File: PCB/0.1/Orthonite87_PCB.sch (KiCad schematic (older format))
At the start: 197 parts

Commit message: PCB schematic updates
add libraries
 schematic progress
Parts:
- added BZ?: Buzzer, PKMCS0909E4000-R1:PKMCS, symbol Keyboard-rescue:Buzzer-Device
- added C? (x2): 10u, keyboard_parts:C_1608, symbol Keyboard-rescue:C-Device
- added C? (x2): 1u, keyboard_parts:C_1608, symbol Keyboard-rescue:C-Device
- added C? (x29): 100n, keyboard_parts:C_1608, symbol Keyboard-rescue:C-Device
- added C? (x2): 4u7, keyboard_parts:C_1608, symbol Keyboard-rescue:C-Device
- added C? (x2): 15p, keyboard_parts:C_1608, symbol Keyboard-rescue:C-Device
- added D?: 1N4148, 1N4148_SOD-123_:SOD3716X135N, symbol Keyboard-rescue:D_Small-Device
- added D?: LE_RED, josh-led:LED_0603_1608Metric_45_noSilk, symbol Keyboard-rescue:LED-Device
- added F?: 500mA, josh-passives-smt:Fuse_0805_2012Metric, symbol Keyboard-rescue:Polyfuse-Device
- added J?: SWD, josh-connectors:STM_4_PIN_THT_Staggered, symbol Keyboard-rescue:Conn_01x04_Male-Connector
- added Q?: DTC123J, DTC123JKAT146:SOT95P280X100-3N, symbol Keyboard-rescue:DTC123J-Transistor_BJT
- added R? (x2): 5k1, keyboard_parts:R_1608, symbol Keyboard-rescue:R-Device
- added R?: 100K, keyboard_parts:R_1608, symbol Keyboard-rescue:R-Device
- added R?: 5K1, keyboard_parts:R_1608, symbol Keyboard-rescue:R-Device
- added SW?: EVQPUL02K, josh-buttons-switches:Panasonic_EVQPUL_EVQPUC, symbol Keyboard-rescue:SW_Push-Switch
- added U?: USBLC6-2SC6, Package_TO_SOT_SMD:SOT-23-6, symbol josh-ic:USBLC6-2SC6
- added U?: AP2112K-3.3, Package_TO_SOT_SMD:SOT-23-5, symbol Keyboard-rescue:AP2112K-3.3-Regulator_Linear
- added U?: STM32F303RCTx, Package_QFP:LQFP-64_10x10mm_P0.5mm, symbol Keyboard-rescue:STM32F303RCTx-MCU_ST_STM32F3
- added Y?: 8MHz, josh-oscillators:Crystal_SMD_3225-4Pin_3.2x2.5mm, symbol Keyboard-rescue:Crystal_GND24-Device
- J?: Notes (none) -> Sub: USB4105-GF-A (available at Digikey)
- gave numbers to parts that had none: 1
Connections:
- net labels added: +3V3-power, +5V-power, BOOT0, BUZZER, GND, SWDCLK, SWDIO, USB+, USB-, USB_D+, USB_D-, VBUS-power, XTAL_0, XTAL_1, nRST
- net labels removed: GND-power
- wire segments 410 -> 593
- no-connect marks 0 -> 2
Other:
- note added: "Bangers r us"
- note added: "DFU/Reset"
- note added: "Programming"
- note added: "The Brains"
- note added: "USB/Power"
- moved on the sheet: D?, K?, SW?

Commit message: Schematic update
Near finished with rev0.1
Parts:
- removed K? (x2): KEYSW, josh-keyboard_W:MXOnly-1U-NoLED, symbol josh-keyboard:MX-NoLED
- added D1, D10, D11, D12, D13, D14, D15, D16, D17, D18, D19, D2, D20, D3, D4, D5, D6, D7, D8, D9: WS2812B, LED_SMD:LED_WS2812B_PLCC4_5.0x5.0mm_P3.2mm, symbol LED:WS2812B
- added D21, D22, D23, D24: SK6812-MINI-E, josh-led:SK8612-MINI-E, symbol josh-led:SK6812-MINI-E
- added D_100, D_15, D_32, D_49, D_66, D_83: 1N4148, 1N4148_SOD-123_:SOD3716X135N, symbol Keyboard-rescue:D_Small-Device
- added K_108: 5,18, josh-keyboard:MXOnly-1U-NoLED, symbol josh-keyboard:MX-NoLED
- added K_16: 0,14, josh-keyboard:MXOnly-1U-NoLED, symbol josh-keyboard:MX-NoLED
- added K_33: 1,17, josh-keyboard:MXOnly-1U-NoLED, symbol josh-keyboard:MX-NoLED
- added K_51: 2,17, josh-keyboard:MXOnly-1U-NoLED, symbol josh-keyboard:MX-NoLED
- added K_53: 3,17, josh-keyboard:MXOnly-1U-NoLED, symbol josh-keyboard:MX-NoLED
- added K_70: 3,18, josh-keyboard:MXOnly-2U-NoLED, symbol josh-keyboard:MX-NoLED
- added K_72: 4,17, josh-keyboard:MXOnly-1U-NoLED, symbol josh-keyboard:MX-NoLED
- added K_89: 4,18, josh-keyboard:MXOnly-2U-NoLED, symbol josh-keyboard:MX-NoLED
- added Q1: BSS138, Package_TO_SOT_SMD:SOT-23, symbol Keyboard-rescue:BSS138-Transistor_FET
- added R1, R2: 10K, keyboard_parts:R_1608, symbol Keyboard-rescue:R-Device
- added R5: 1K5, Resistor_SMD:R_0603_1608Metric, symbol Device:R_Small
- BZ1: renamed from BZ?; footprint PKMCS0909E4000-R1:PKMCS -> Buzzer_Beeper:Buzzer_Murata_PKMCS0909E4000-R1
- K_1: renamed from K?; value Encoder_MX -> 0,15
- K_10: renamed from K?; value KEYSW -> 0,8; footprint josh-keyboard_W:MXOnly-1U-NoLED -> josh-keyboard:MXOnly-1U-NoLED
- K_100: renamed from K?; value KEYSW -> 5,9; footprint josh-keyboard_W:MXOnly-1U-NoLED -> josh-keyboard:MXOnly-1U-NoLED
- K_101: renamed from K?; value KEYSW -> 5,10; footprint josh-keyboard_W:MXOnly-1U-NoLED -> josh-keyboard:MXOnly-1U-NoLED
- K_102: renamed from K?; value KEYSW -> 5,11; footprint josh-keyboard_W:MXOnly-1U-NoLED -> josh-keyboard:MXOnly-1U-NoLED
- K_103: renamed from K?; value KEYSW -> 5,12; footprint josh-keyboard_W:MXOnly-1U-NoLED -> josh-keyboard:MXOnly-1U-NoLED
- K_104: renamed from K?; value KEYSW -> 5,14; footprint josh-keyboard_W:MXOnly-1U-NoLED -> josh-keyboard:MXOnly-3U-ReversedStabilizers-NoLED
- K_105: renamed from K?; value KEYSW -> 5,15; footprint josh-keyboard_W:MXOnly-1U-NoLED -> josh-keyboard:MXOnly-1U-NoLED
- K_106: renamed from K?; value KEYSW -> 5,16; footprint josh-keyboard_W:MXOnly-1U-NoLED -> josh-keyboard:MXOnly-1U-NoLED
- K_107: renamed from K?; value KEYSW -> 5,17; footprint josh-keyboard_W:MXOnly-1U-NoLED -> josh-keyboard:MXOnly-1U-NoLED
- K_11: renamed from K?; value KEYSW -> 0,9; footprint josh-keyboard_W:MXOnly-1U-NoLED -> josh-keyboard:MXOnly-1U-NoLED
- K_12: renamed from K?; value KEYSW -> 0,10; footprint josh-keyboard_W:MXOnly-1U-NoLED -> josh-keyboard:MXOnly-1U-NoLED
- K_13: renamed from K?; value KEYSW -> 0,11; footprint josh-keyboard_W:MXOnly-1U-NoLED -> josh-keyboard:MXOnly-1U-NoLED
- K_14: renamed from K?; value KEYSW -> 0,12; footprint josh-keyboard_W:MXOnly-1U-NoLED -> josh-keyboard:MXOnly-1U-NoLED
- K_15: renamed from K?; value KEYSW -> 0,13; footprint josh-keyboard_W:MXOnly-1U-NoLED -> josh-keyboard:MXOnly-1U-NoLED
- K_17: renamed from K?; value KEYSW -> 1,15; footprint josh-keyboard_W:MXOnly-1U-NoLED -> josh-keyboard:MXOnly-1U-NoLED
- K_18: renamed from K?; value KEYSW -> 1,1; footprint josh-keyboard_W:MXOnly-1U-NoLED -> josh-keyboard:MXOnly-1U-NoLED
- K_19: renamed from K?; value KEYSW -> 1,2; footprint josh-keyboard_W:MXOnly-1U-NoLED -> josh-keyboard:MXOnly-1U-NoLED
- K_2: renamed from K?; value KEYSW -> 0,0; footprint josh-keyboard_W:MXOnly-1U-NoLED -> josh-keyboard:MXOnly-1U-NoLED
- K_20: renamed from K?; value KEYSW -> 1,3; footprint josh-keyboard_W:MXOnly-1U-NoLED -> josh-keyboard:MXOnly-1U-NoLED
- K_21: renamed from K?; value KEYSW -> 1,4; footprint josh-keyboard_W:MXOnly-1U-NoLED -> josh-keyboard:MXOnly-1U-NoLED
- K_22: renamed from K?; value KEYSW -> 1,5; footprint josh-keyboard_W:MXOnly-1U-NoLED -> josh-keyboard:MXOnly-1U-NoLED
- K_23: renamed from K?; value KEYSW -> 1,6; footprint josh-keyboard_W:MXOnly-1U-NoLED -> josh-keyboard:MXOnly-1U-NoLED
- K_24: renamed from K?; value KEYSW -> 1,7; footprint josh-keyboard_W:MXOnly-1U-NoLED -> josh-keyboard:MXOnly-1U-NoLED
- K_25: renamed from K?; value KEYSW -> 1,8; footprint josh-keyboard_W:MXOnly-1U-NoLED -> josh-keyboard:MXOnly-1U-NoLED
- K_26: renamed from K?; value KEYSW -> 1,9; footprint josh-keyboard_W:MXOnly-1U-NoLED -> josh-keyboard:MXOnly-1U-NoLED
- K_27: renamed from K?; value KEYSW -> 1,10; footprint josh-keyboard_W:MXOnly-1U-NoLED -> josh-keyboard:MXOnly-1U-NoLED
- K_28: renamed from K?; value KEYSW -> 1,11; footprint josh-keyboard_W:MXOnly-1U-NoLED -> josh-keyboard:MXOnly-1U-NoLED
- K_29: renamed from K?; value KEYSW -> 1,12; footprint josh-keyboard_W:MXOnly-1U-NoLED -> josh-keyboard:MXOnly-1U-NoLED
- K_3: renamed from K?; value KEYSW -> 0,1; footprint josh-keyboard_W:MXOnly-1U-NoLED -> josh-keyboard:MXOnly-1U-NoLED
- K_30: renamed from K?; value KEYSW -> 1,13; footprint josh-keyboard_W:MXOnly-1U-NoLED -> josh-keyboard:MXOnly-1U-NoLED
- K_31: renamed from K?; value KEYSW -> 1,14; footprint josh-keyboard_W:MXOnly-1U-NoLED -> josh-keyboard:MXOnly-1U-NoLED
- K_32: renamed from K?; value KEYSW -> 1,16; footprint josh-keyboard_W:MXOnly-1U-NoLED -> josh-keyboard:MXOnly-2U-NoLED
- K_34: renamed from K?; value KEYSW -> 2,1; footprint josh-keyboard_W:MXOnly-1U-NoLED -> josh-keyboard:MXOnly-1U-NoLED
- K_35: renamed from K?; value KEYSW -> 2,0; footprint josh-keyboard_W:MXOnly-1U-NoLED -> josh-keyboard:MXOnly-1U-NoLED
- K_36: renamed from K?; value KEYSW -> 2,2; footprint josh-keyboard_W:MXOnly-1U-NoLED -> josh-keyboard:MXOnly-2U-NoLED
- K_37: renamed from K?; value KEYSW -> 2,3; footprint josh-keyboard_W:MXOnly-1U-NoLED -> josh-keyboard:MXOnly-1U-NoLED
- K_38: renamed from K?; value KEYSW -> 2,4; footprint josh-keyboard_W:MXOnly-1U-NoLED -> josh-keyboard:MXOnly-1U-NoLED
- K_39: renamed from K?; value KEYSW -> 2,5; footprint josh-keyboard_W:MXOnly-1U-NoLED -> josh-keyboard:MXOnly-1U-NoLED
- K_4: renamed from K?; value KEYSW -> 0,2; footprint josh-keyboard_W:MXOnly-1U-NoLED -> josh-keyboard:MXOnly-1U-NoLED
- K_40: renamed from K?; value KEYSW -> 2,6; footprint josh-keyboard_W:MXOnly-1U-NoLED -> josh-keyboard:MXOnly-1U-NoLED
- K_41: renamed from K?; value KEYSW -> 2,7; footprint josh-keyboard_W:MXOnly-1U-NoLED -> josh-keyboard:MXOnly-1U-NoLED
- K_42: renamed from K?; value KEYSW -> 2,8; footprint josh-keyboard_W:MXOnly-1U-NoLED -> josh-keyboard:MXOnly-1U-NoLED
- K_43: renamed from K?; value KEYSW -> 2,9; footprint josh-keyboard_W:MXOnly-1U-NoLED -> josh-keyboard:MXOnly-1U-NoLED
- K_44: renamed from K?; value KEYSW -> 2,10; footprint josh-keyboard_W:MXOnly-1U-NoLED -> josh-keyboard:MXOnly-1U-NoLED
- K_45: renamed from K?; value KEYSW -> 2,11; footprint josh-keyboard_W:MXOnly-1U-NoLED -> josh-keyboard:MXOnly-1U-NoLED
- K_46: renamed from K?; value KEYSW -> 2,12; footprint josh-keyboard_W:MXOnly-1U-NoLED -> josh-keyboard:MXOnly-1U-NoLED
- K_47: renamed from K?; value KEYSW -> 2,13; footprint josh-keyboard_W:MXOnly-1U-NoLED -> josh-keyboard:MXOnly-1U-NoLED
- K_48: renamed from K?; value KEYSW -> 2,14; footprint josh-keyboard_W:MXOnly-1U-NoLED -> josh-keyboard:MXOnly-1U-NoLED
- K_49: renamed from K?; value KEYSW -> 2,15; footprint josh-keyboard_W:MXOnly-1U-NoLED -> josh-keyboard:MXOnly-1U-NoLED
- K_5: renamed from K?; value KEYSW -> 0,3; footprint josh-keyboard_W:MXOnly-1U-NoLED -> josh-keyboard:MXOnly-1U-NoLED
- K_50: renamed from K?; value KEYSW -> 2,16; footprint josh-keyboard_W:MXOnly-1U-NoLED -> josh-keyboard:MXOnly-1U-NoLED
- K_52: renamed from K?; value KEYSW -> 3,1; footprint josh-keyboard_W:MXOnly-1U-NoLED -> josh-keyboard:MXOnly-1U-NoLED
- K_54: renamed from K?; value KEYSW -> 3,0; footprint josh-keyboard_W:MXOnly-1U-NoLED -> josh-keyboard:MXOnly-1U-NoLED
- K_55: renamed from K?; value KEYSW -> 3,2; footprint josh-keyboard_W:MXOnly-1U-NoLED -> josh-keyboard:MXOnly-2U-NoLED
- K_56: renamed from K?; value KEYSW -> 3,3; footprint josh-keyboard_W:MXOnly-1U-NoLED -> josh-keyboard:MXOnly-1U-NoLED
- K_57: renamed from K?; value KEYSW -> 3,4; footprint josh-keyboard_W:MXOnly-1U-NoLED -> josh-keyboard:MXOnly-1U-NoLED
- K_58: renamed from K?; value KEYSW -> 3,5; footprint josh-keyboard_W:MXOnly-1U-NoLED -> josh-keyboard:MXOnly-1U-NoLED
- K_59: renamed from K?; value KEYSW -> 3,6; footprint josh-keyboard_W:MXOnly-1U-NoLED -> josh-keyboard:MXOnly-1U-NoLED
- K_6: renamed from K?; value KEYSW -> 0,4; footprint josh-keyboard_W:MXOnly-1U-NoLED -> josh-keyboard:MXOnly-1U-NoLED
- K_60: renamed from K?; value KEYSW -> 3,7; footprint josh-keyboard_W:MXOnly-1U-NoLED -> josh-keyboard:MXOnly-1U-NoLED
- K_61: renamed from K?; value KEYSW -> 3,8; footprint josh-keyboard_W:MXOnly-1U-NoLED -> josh-keyboard:MXOnly-1U-NoLED
- K_62: renamed from K?; value KEYSW -> 3,9; footprint josh-keyboard_W:MXOnly-1U-NoLED -> josh-keyboard:MXOnly-1U-NoLED
- K_63: renamed from K?; value KEYSW -> 3,10; footprint josh-keyboard_W:MXOnly-1U-NoLED -> josh-keyboard:MXOnly-1U-NoLED
- K_64: renamed from K?; value KEYSW -> 3,11; footprint josh-keyboard_W:MXOnly-1U-NoLED -> josh-keyboard:MXOnly-1U-NoLED
- K_65: renamed from K?; value KEYSW -> 3,12; footprint josh-keyboard_W:MXOnly-1U-NoLED -> josh-keyboard:MXOnly-1U-NoLED
- K_66: renamed from K?; value KEYSW -> 3,13; footprint josh-keyboard_W:MXOnly-1U-NoLED -> josh-keyboard:MXOnly-1U-NoLED
- K_67: renamed from K?; value KEYSW -> 3,14; footprint josh-keyboard_W:MXOnly-1U-NoLED -> josh-keyboard:MXOnly-1U-NoLED
- K_68: renamed from K?; value KEYSW -> 3,15; footprint josh-keyboard_W:MXOnly-1U-NoLED -> josh-keyboard:MXOnly-1U-NoLED
- K_69: renamed from K?; value KEYSW -> 3,16; footprint josh-keyboard_W:MXOnly-1U-NoLED -> josh-keyboard:MXOnly-1U-NoLED
- K_7: renamed from K?; value KEYSW -> 0,5; footprint josh-keyboard_W:MXOnly-1U-NoLED -> josh-keyboard:MXOnly-1U-NoLED
- K_71: renamed from K?; value KEYSW -> 4,1; footprint josh-keyboard_W:MXOnly-1U-NoLED -> josh-keyboard:MXOnly-1U-NoLED
- K_73: renamed from K?; value KEYSW -> 4,0; footprint josh-keyboard_W:MXOnly-1U-NoLED -> josh-keyboard:MXOnly-1U-NoLED
- K_74: renamed from K?; value KEYSW -> 4,2; footprint josh-keyboard_W:MXOnly-1U-NoLED -> josh-keyboard:MXOnly-2U-NoLED
- K_75: renamed from K?; value KEYSW -> 4,3; footprint josh-keyboard_W:MXOnly-1U-NoLED -> josh-keyboard:MXOnly-1U-NoLED
- K_76: renamed from K?; value KEYSW -> 4,4; footprint josh-keyboard_W:MXOnly-1U-NoLED -> josh-keyboard:MXOnly-1U-NoLED
- K_77: renamed from K?; value KEYSW -> 4,5; footprint josh-keyboard_W:MXOnly-1U-NoLED -> josh-keyboard:MXOnly-1U-NoLED
- K_78: renamed from K?; value KEYSW -> 4,6; footprint josh-keyboard_W:MXOnly-1U-NoLED -> josh-keyboard:MXOnly-1U-NoLED
- K_79: renamed from K?; value KEYSW -> 4,7; footprint josh-keyboard_W:MXOnly-1U-NoLED -> josh-keyboard:MXOnly-1U-NoLED
- K_8: renamed from K?; value KEYSW -> 0,6; footprint josh-keyboard_W:MXOnly-1U-NoLED -> josh-keyboard:MXOnly-1U-NoLED
- K_80: renamed from K?; value KEYSW -> 4,8; footprint josh-keyboard_W:MXOnly-1U-NoLED -> josh-keyboard:MXOnly-1U-NoLED
- K_81: renamed from K?; value KEYSW -> 4,9; footprint josh-keyboard_W:MXOnly-1U-NoLED -> josh-keyboard:MXOnly-1U-NoLED
- K_82: renamed from K?; value KEYSW -> 4,10; footprint josh-keyboard_W:MXOnly-1U-NoLED -> josh-keyboard:MXOnly-1U-NoLED
- K_83: renamed from K?; value KEYSW -> 4,11; footprint josh-keyboard_W:MXOnly-1U-NoLED -> josh-keyboard:MXOnly-1U-NoLED
- K_84: renamed from K?; value KEYSW -> 4,12; footprint josh-keyboard_W:MXOnly-1U-NoLED -> josh-keyboard:MXOnly-1U-NoLED
- K_85: renamed from K?; value KEYSW -> 4,13; footprint josh-keyboard_W:MXOnly-1U-NoLED -> josh-keyboard:MXOnly-1U-NoLED
- K_86: renamed from K?; value KEYSW -> 4,14; footprint josh-keyboard_W:MXOnly-1U-NoLED -> josh-keyboard:MXOnly-1U-NoLED
- K_87: renamed from K?; value KEYSW -> 4,15; footprint josh-keyboard_W:MXOnly-1U-NoLED -> josh-keyboard:MXOnly-1U-NoLED
- K_88: renamed from K?; value KEYSW -> 4,16; footprint josh-keyboard_W:MXOnly-1U-NoLED -> josh-keyboard:MXOnly-1U-NoLED
- K_9: renamed from K?; value KEYSW -> 0,7; footprint josh-keyboard_W:MXOnly-1U-NoLED -> josh-keyboard:MXOnly-1U-NoLED
- K_90: renamed from K?; value KEYSW -> 5,4; footprint josh-keyboard_W:MXOnly-1U-NoLED -> josh-keyboard:MXOnly-1U-NoLED
- K_91: renamed from K?; value KEYSW -> 5,13; footprint josh-keyboard_W:MXOnly-1U-NoLED -> josh-keyboard:MXOnly-1U-NoLED
- K_92: renamed from K?; value KEYSW -> 5,0; footprint josh-keyboard_W:MXOnly-1U-NoLED -> josh-keyboard:MXOnly-1U-NoLED
- K_93: renamed from K?; value KEYSW -> 5,1; footprint josh-keyboard_W:MXOnly-1U-NoLED -> josh-keyboard:MXOnly-1U-NoLED
- K_94: renamed from K?; value KEYSW -> 5,2; footprint josh-keyboard_W:MXOnly-1U-NoLED -> josh-keyboard:MXOnly-1U-NoLED
- K_95: renamed from K?; value KEYSW -> 5,3; footprint josh-keyboard_W:MXOnly-1U-NoLED -> josh-keyboard:MXOnly-1U-NoLED
- K_96: renamed from K?; value KEYSW -> 5,5; footprint josh-keyboard_W:MXOnly-1U-NoLED -> josh-keyboard:MXOnly-3U-ReversedStabilizers-NoLED
- K_97: renamed from K?; value KEYSW -> 5,6; footprint josh-keyboard_W:MXOnly-1U-NoLED -> josh-keyboard:MXOnly-1U-NoLED
- K_98: renamed from K?; value KEYSW -> 5,7; footprint josh-keyboard_W:MXOnly-1U-NoLED -> josh-keyboard:MXOnly-1U-NoLED
- K_99: renamed from K?; value KEYSW -> 5,8; footprint josh-keyboard_W:MXOnly-1U-NoLED -> josh-keyboard:MXOnly-1U-NoLED
- gave numbers to parts that had none: 146
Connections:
- net labels added: +3.3V, +3V3, +5V, VBUS, col16, underglow
- net labels removed: +5V-power, VBUS-power
- wire segments 593 -> 721
- no-connect marks 2 -> 22
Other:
- note added: "3v3 -> 5v logic shift"
- note added: "Status"
- note added: "Underglow"
- moved on the sheet: C1, C10, C11, C2, C3, C4, C5, C6, C7, C8, C9, D_1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

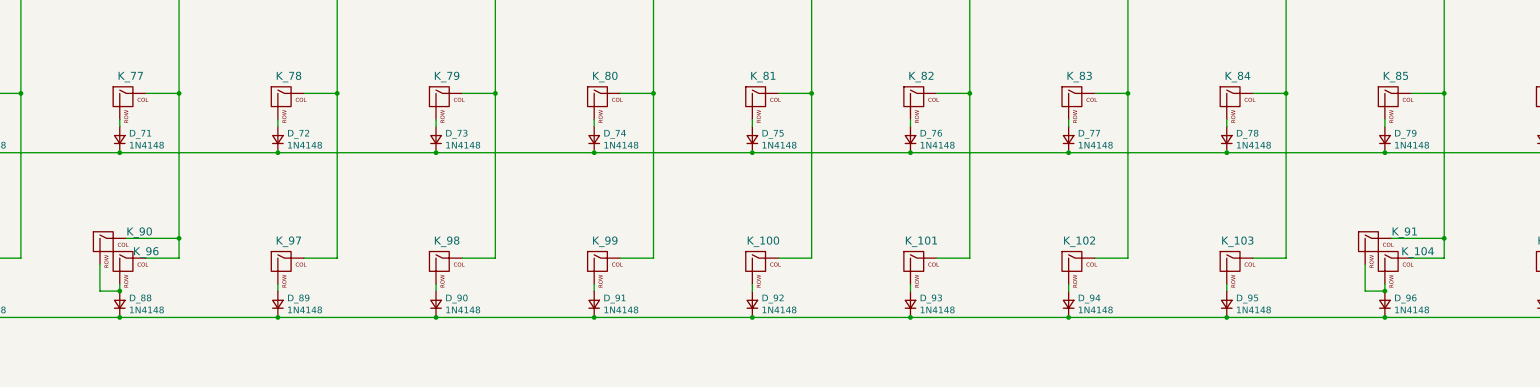
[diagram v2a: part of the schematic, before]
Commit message: pcb routing and art
Finished routing and rev1 of art  on pcb
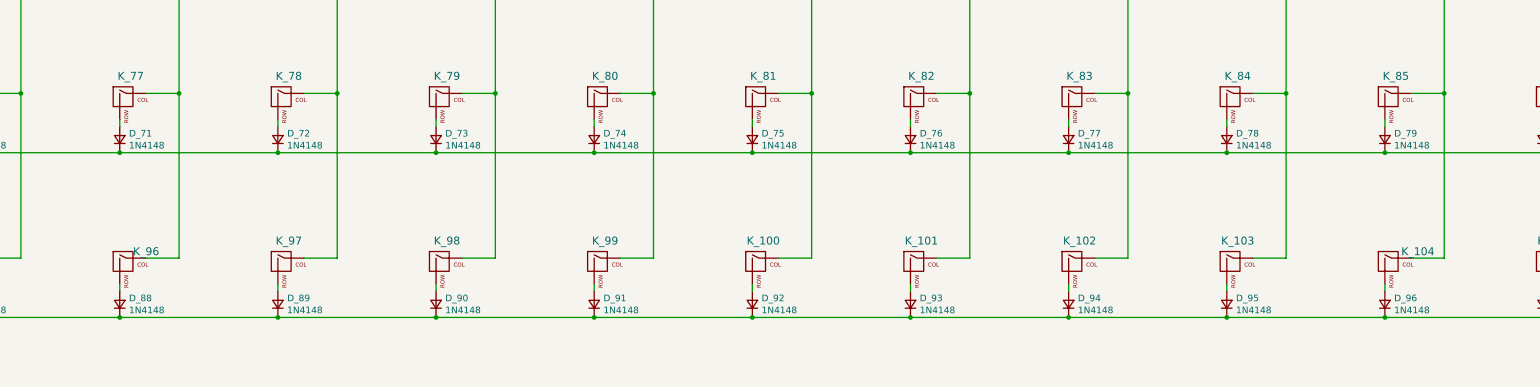
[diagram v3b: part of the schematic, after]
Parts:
- removed K_90: 5,4, josh-keyboard:MXOnly-1U-NoLED, symbol josh-keyboard:MX-NoLED
- removed K_91: 5,13, josh-keyboard:MXOnly-1U-NoLED, symbol josh-keyboard:MX-NoLED

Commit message: Updates
bug fixes
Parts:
- R5: JLCSMT (none) -> C22843; LCSC (none) -> C22843; MPN (none) -> C22843; Manufacturer (none) -> Uniroyal Elec
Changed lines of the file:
@@
 F 2 "Resistor_SMD:R_0603_1608Metric" H 22200 12300 50  0001 C CNN
 F 3 "~" H 22200 12300 50  0001 C CNN
+F 4 "C22843" H 22200 12300 50  0001 C CNN "JLCSMT"
+F 5 "C22843" H 22200 12300 50  0001 C CNN "LCSC"
+F 6 "C22843" H 22200 12300 50  0001 C CNN "MPN"
+F 7 "Uniroyal Elec" H 22200 12300 50  0001 C CNN "Manufacturer"
 	1    22200 12300
 	1    0    0    -1
